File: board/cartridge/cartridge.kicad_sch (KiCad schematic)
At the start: 33 parts, among them J1 WQ21823-DES1-7F, J2 KH-TYPE-C-16P, J3 TC2030-NL, P1 Card Edge, SW1 K3-1410S, SW2 K3-1410S, U1 AMS1117-3.3, U2 STM32G0B0RETx, U4 NAU8814Y, Y1 X322516MLB4SI

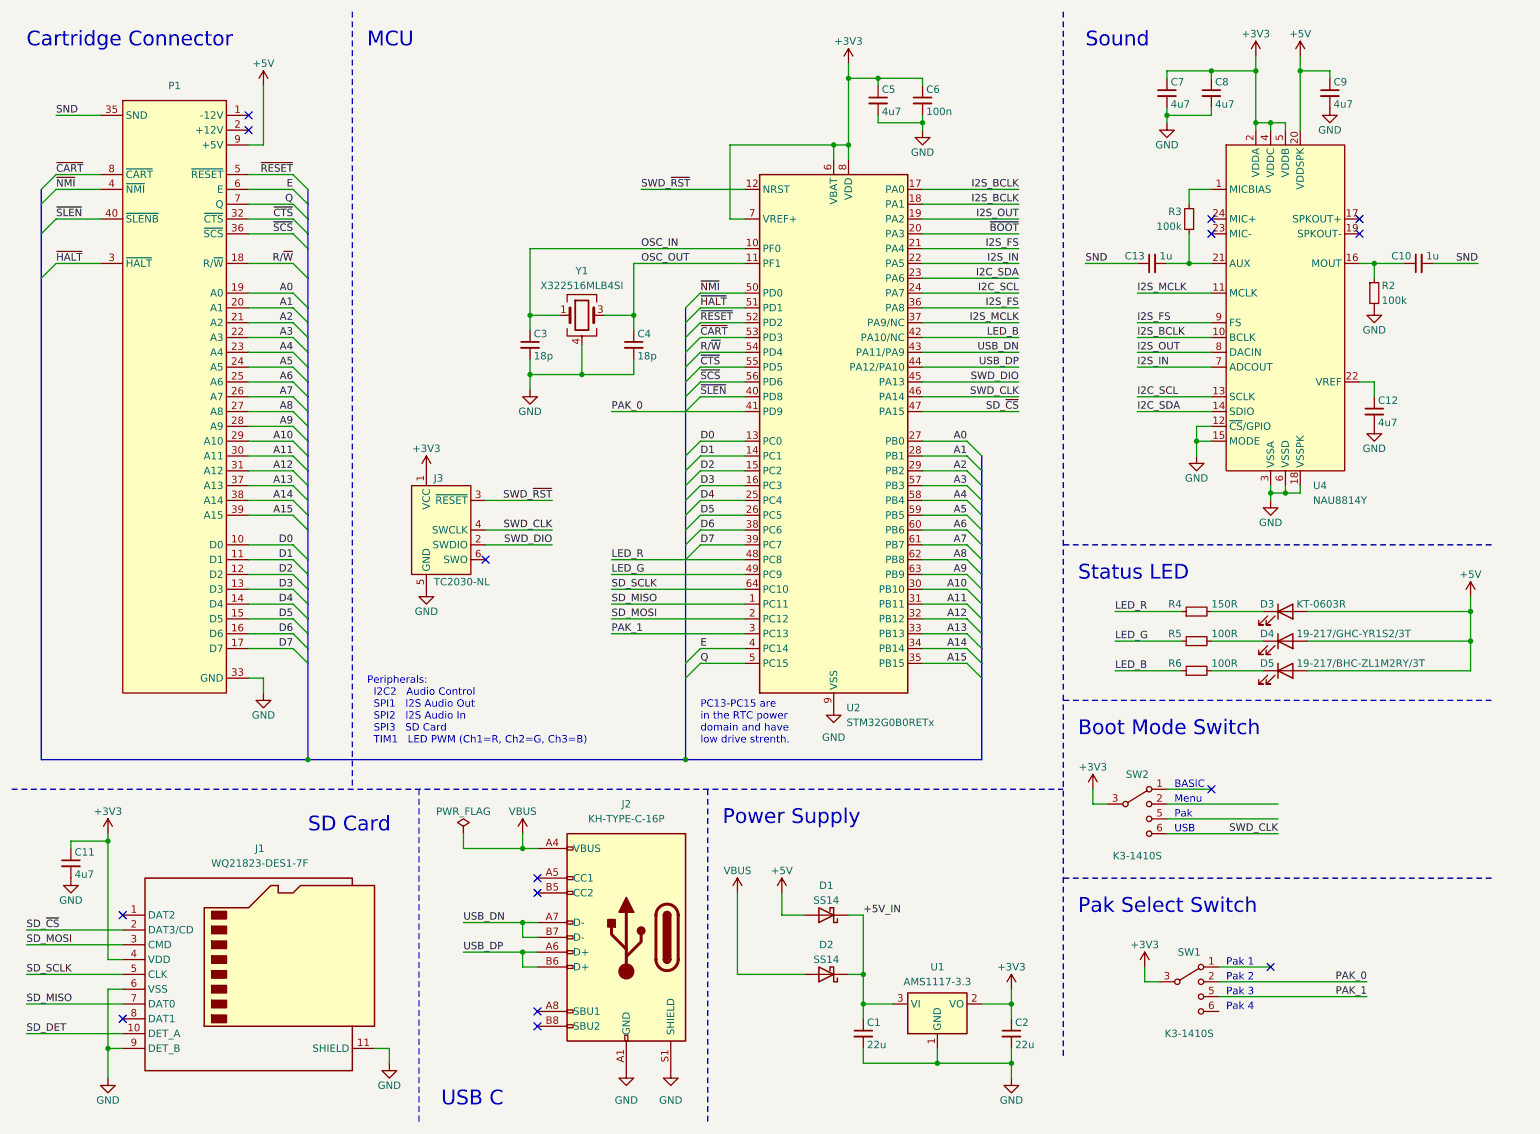
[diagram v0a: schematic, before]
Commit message: Move pin assignments around to accomodate new switches.
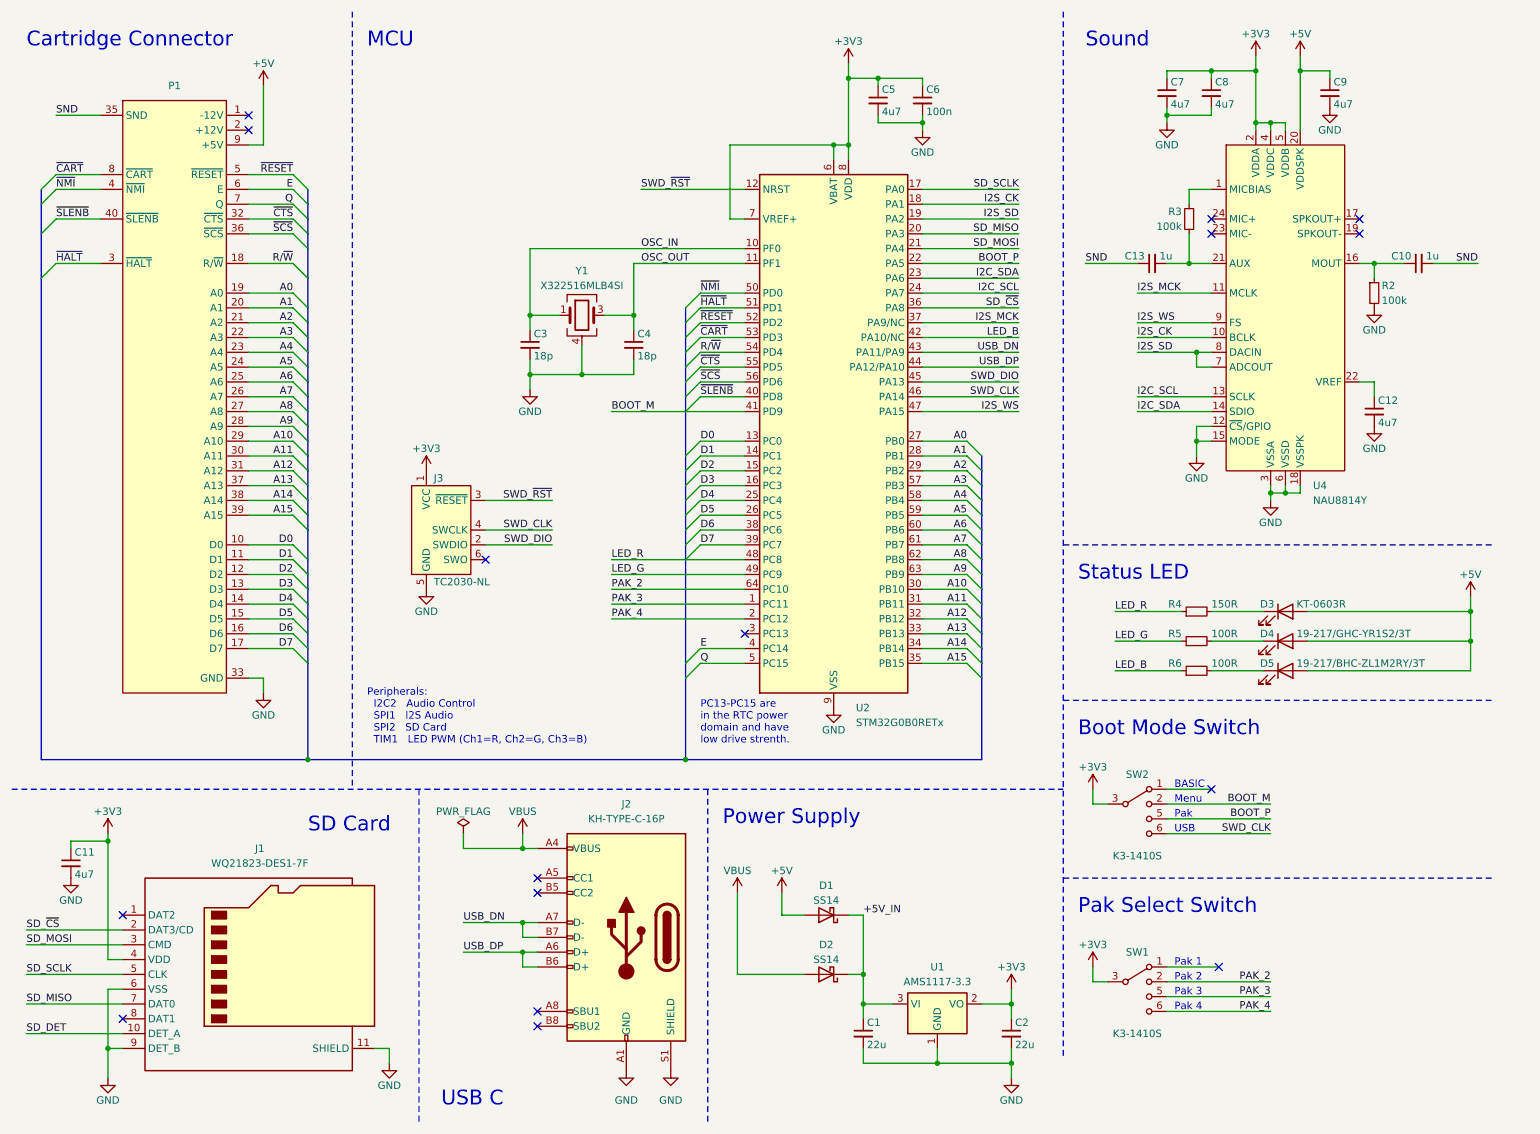
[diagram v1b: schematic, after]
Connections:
- net I2S_OUT is gone; now on net I2S_SD: U2.19 (PA2), U4.8 (DACIN)
- net ~{BOOT} is gone; now on net SD_MISO: U2.20 (PA3)
- net SD_MISO: no longer U2.1 (PC11)
- net SD_MOSI: now also U2.21 (PA4); no longer U2.2 (PC12)
- net SD_SCLK: now also U2.17 (PA0); no longer U2.64 (PC10)
- net SD_~{CS}: now also U2.36 (PA8); no longer U2.47 (PA15)
- net PAK_4: now reaches SW1.6 (4)
- net PAK_4: now also U2.2 (PC12)
- net BOOT_M: now reaches SW2.2
- net BOOT_M: now also U2.41 (PD9)
- net BOOT_P: now reaches SW2.5 (3)
- net BOOT_P: now also U2.22 (PA5)
- net I2S_BCLK renamed I2S_CK
- net I2S_CK: no longer U2.17 (PA0)
- removed net I2S_FS: U2.21 (PA4), U2.36 (PA8), U4.9 (FS)
- net I2S_IN renamed I2S_SD
- net I2S_SD: no longer U2.22 (PA5)
- net I2S_MCLK renamed I2S_MCK
- net PAK_0 renamed PAK_2
- net PAK_2: now also U2.64 (PC10); no longer U2.41 (PD9)
- net PAK_1: no longer names the net of U2.3 (PC13)
- net PAK_1: no longer SW1.5 (3)
- net ~{SLEN} renamed ~{SLENB}
- new net I2S_WS: U2.47 (PA15), U4.9 (FS)
- new net PAK_3: SW1.5 (3), U2.1 (PC11)
- no-connect marks 15 -> 16
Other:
- note added: "Peripherals: I2C2 Audio Control SPI1 I2S Audio SPI2 SD Card TIM1 LED PWM (Ch1=R, Ch2=G, Ch3=B)"
- note removed: "Peripherals: I2C2 Audio Control SPI1 I2S Audio Out SPI2 I2S Audio In SPI3 SD Card TIM1 LED PWM (Ch1=R, Ch2=G, Ch3=B)"
- moved on the sheet: SW1

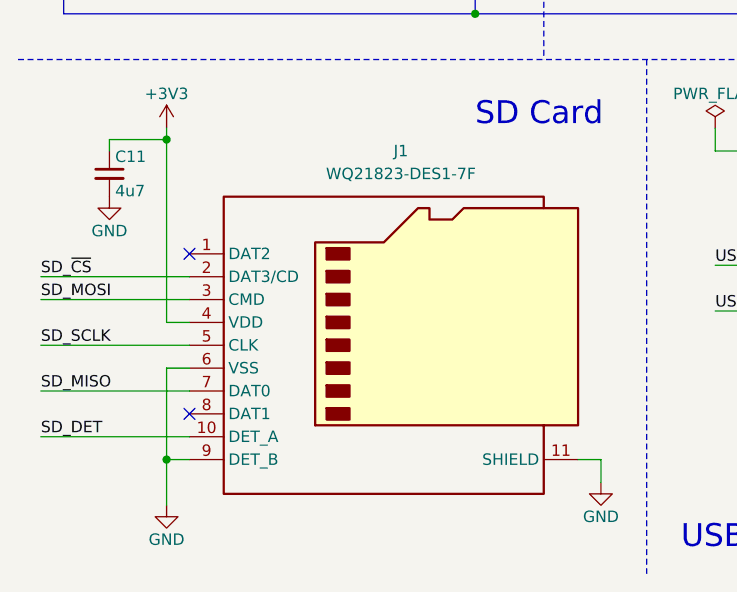
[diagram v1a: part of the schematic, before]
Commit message: Switch to cheaper SD card socket, more routing.
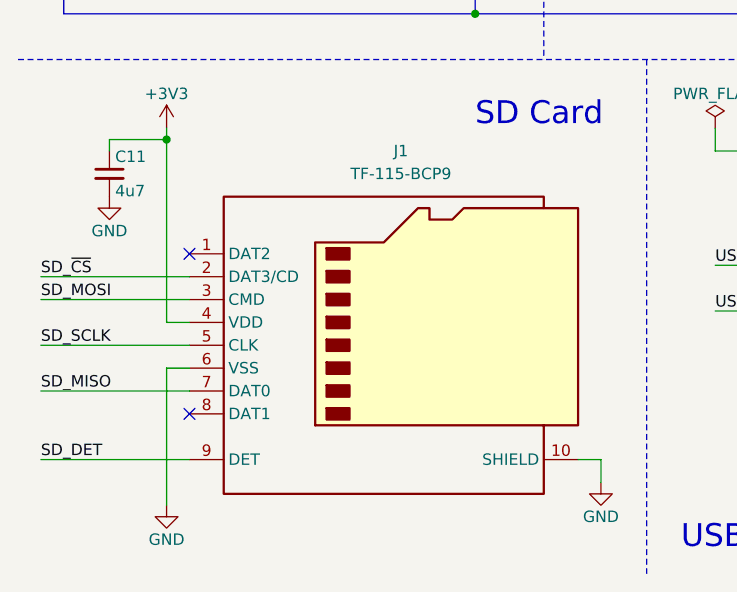
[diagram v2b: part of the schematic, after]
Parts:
- J1: value WQ21823-DES1-7F -> TF-115-BCP9; footprint 0Project:Foxconn_WQ21823-DES1-7F -> 0Project:XUNPU_TF-115-BCP9; symbol Connector:Micro_SD_Card_Det2 -> Connector:Micro_SD_Card_Det1; LCSC C426216 -> C720505
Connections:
- net GND: now also J1.10 (SHIELD); no longer J1.11 (SHIELD), J1.9 (DET_B)
- net SD_DET: now also J1.9 (DET); no longer J1.10 (DET_A)
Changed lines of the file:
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@@
   (junction (at 101.6 74.93) (diameter 0) (color 0 0 0 0)
-  )
-  (junction (at 29.21 190.5) (diameter 0) (color 0 0 0 0)
   )
   (junction (at 210.82 30.48) (diameter 0) (color 0 0 0 0)
@@
     (stroke (width 0) (type default))
   )
-  (wire (pts (xy 15.24 187.96) (xy 31.75 187.96))
+  (wire (pts (xy 15.24 190.5) (xy 31.75 190.5))
     (stroke (width 0) (type default))
   )
@@
     (stroke (width 0) (type default))
   )
-  (wire (pts (xy 29.21 190.5) (xy 31.75 190.5))
-    (stroke (width 0) (type default))
-  )
   (wire (pts (xy 168.91 63.5) (xy 185.42 63.5))
     (stroke (width 0) (type default))
@@
     (stroke (width 0) (type default))
   )
-  (wire (pts (xy 29.21 190.5) (xy 29.21 195.58))
-    (stroke (width 0) (type default))
-  )
   (wire (pts (xy 29.21 153.67) (xy 29.21 154.94))
     (stroke (width 0) (type default))
@@
     (stroke (width 0) (type default))
   )
-  (wire (pts (xy 29.21 180.34) (xy 29.21 190.5))
+  (wire (pts (xy 29.21 180.34) (xy 29.21 195.58))
     (stroke (width 0) (type default))
   )
@@
     (effects (font (size 1.27 1.27)) (justify right bottom))
   )
-  (label "SD_DET" (at 15.24 187.96 0) (fields_autoplaced)
+  (label "SD_DET" (at 15.24 190.5 0) (fields_autoplaced)
     (effects (font (size 1.27 1.27)) (justify left bottom))
   )
@@
     )
   )
-  (symbol (lib_id "Connector:Micro_SD_Card_Det2") (at 54.61 177.8 0) (unit 1)
+  (symbol (lib_id "Connector:Micro_SD_Card_Det1") (at 54.61 177.8 0) (unit 1)
     (in_bom yes) (on_board yes) (dnp no) (fields_autoplaced)
     (property "Reference" "J1" (at 55.245 156.21 0)
       (effects (font (size 1.27 1.27)))
     )
-    (property "Value" "WQ21823-DES1-7F" (at 55.245 158.75 0)
-      (effects (font (size 1.27 1.27)))
-    )
-    (property "Footprint" "0Project:Foxconn_WQ21823-DES1-7F" (at 106.68 160.02 0)
-      (effects (font (size 1.27 1.27)) hide)
-    )
-    (property "Datasheet" "https://datasheet.lcsc.com/lcsc/1912111437_FOXCONN-WQ21823-DES1-7F_C426216.pdf" (at 57.15 175.26 0)
-      (effects (font (size 1.27 1.27)) hide)
-    )
-    (property "LCSC" "C426216" (at 54.61 177.8 0)
+    (property "Value" "TF-115-BCP9" (at 55.245 158.75 0)
+      (effects (font (size 1.27 1.27)))
+    )
+    (property "Footprint" "0Project:XUNPU_TF-115-BCP9" (at 106.68 160.02 0)
+      (effects (font (size 1.27 1.27)) hide)
+    )
+    (property "Datasheet" "https://datasheet.lcsc.com/lcsc/2109061830_XUNPU-TF-115-BCP9_C720505.pdf" (at 54.61 175.26 0)
+      (effects (font (size 1.27 1.27)) hide)
+    )
+    (property "LCSC" "C720505" (at 54.61 177.8 0)
       (effects (font (size 1.27 1.27)) hide)
     )
@@
     (pin "2")
     (pin "10")
-    (pin "11")
     (pin "3")
     (pin "1")
